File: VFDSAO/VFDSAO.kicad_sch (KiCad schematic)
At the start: 4 parts, among them U1 CH32V003FxPx, U2 HV5812, X1 Simple_Addon_v2

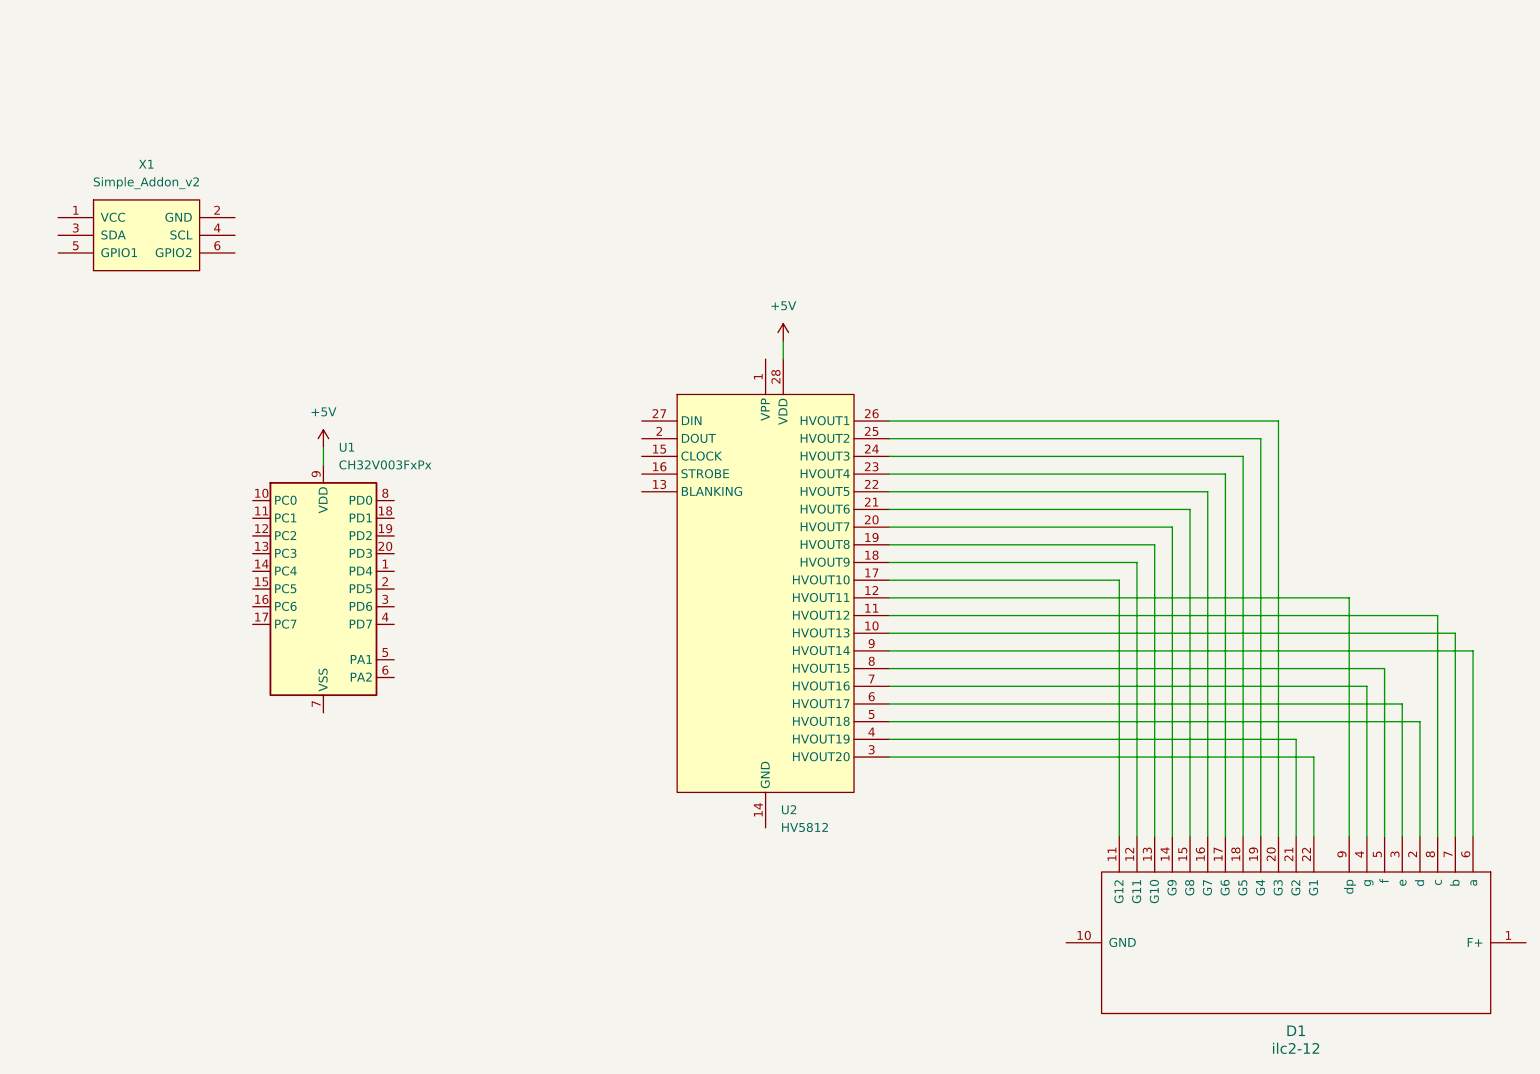
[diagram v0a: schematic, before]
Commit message: Adding I2C level shifters
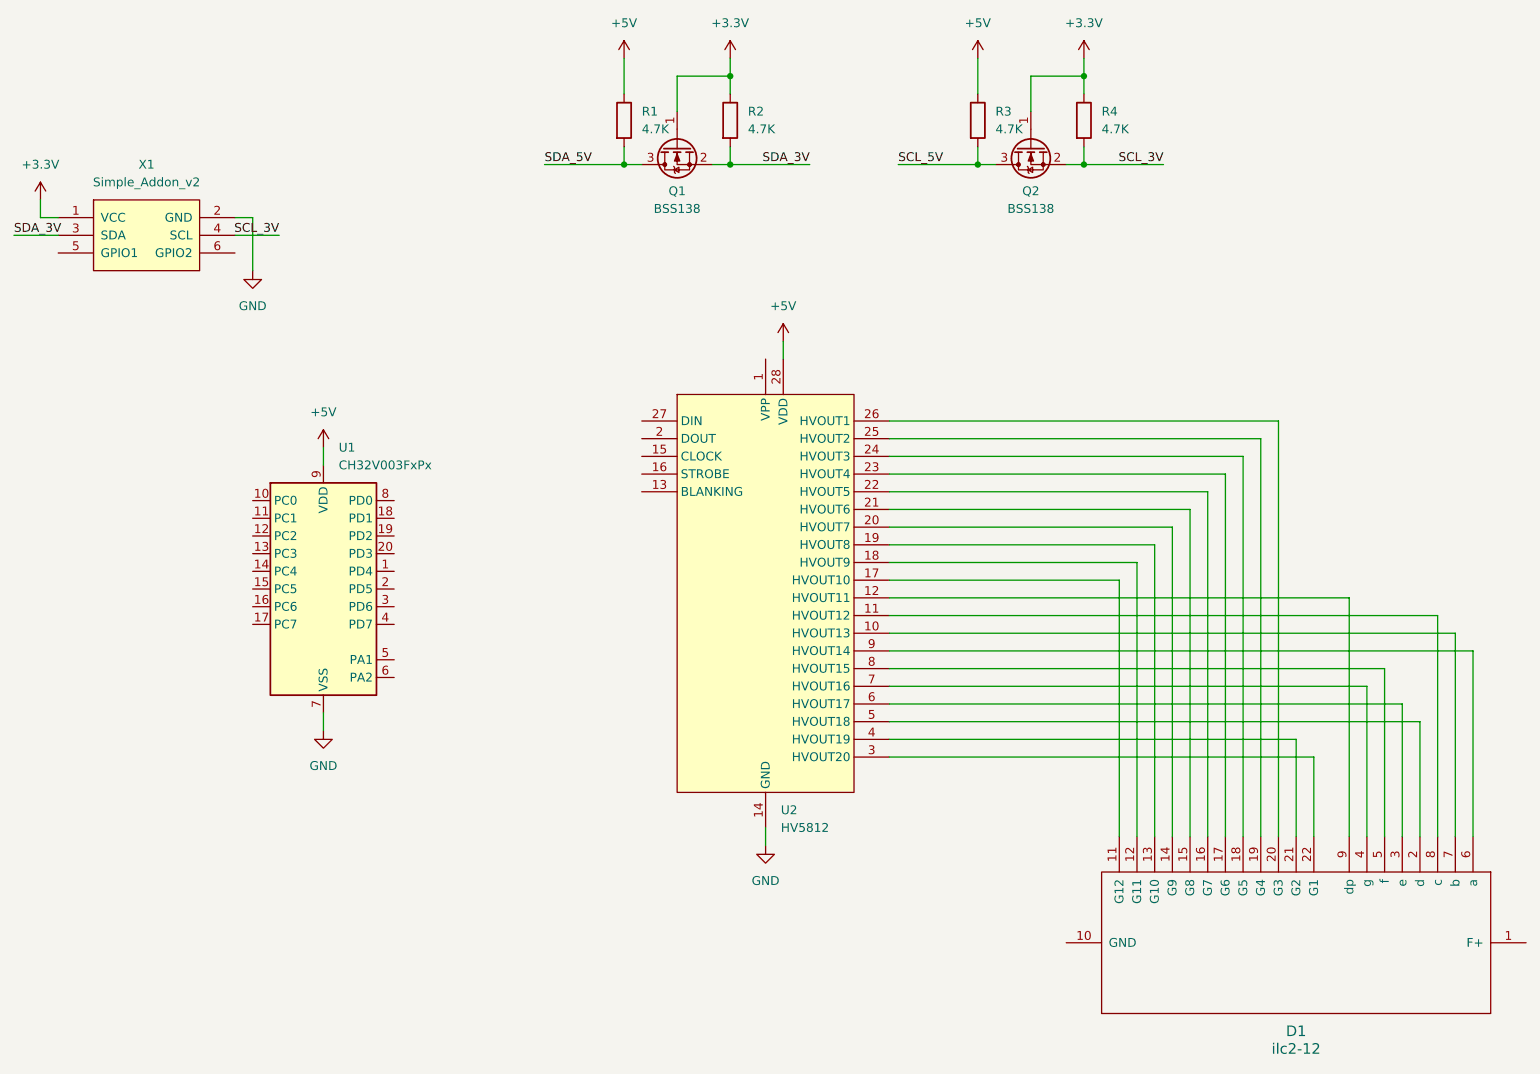
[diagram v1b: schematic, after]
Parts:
- added Q1, Q2: BSS138, Package_TO_SOT_SMD:SOT-23, symbol Transistor_FET:BSS138
- added R1, R2, R3, R4: 4.7K, symbol Device:R
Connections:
- net +5V: now also R1.1, R3.1
- net GND: now reaches U2.14 (GND)
- net GND: now also U1.7 (VSS), X1.2 (GND)
- net +3.3V: now reaches X1.1 (VCC)
- net +3.3V: now also Q1.1 (G), Q2.1 (G), R2.1, R4.1
- net SDA_3V: now reaches X1.3 (SDA)
- net SDA_3V: now also Q1.2 (S), R2.2
- net SCL_3V: now reaches X1.4 (SCL)
- net SCL_3V: now also Q2.2 (S), R4.2
- new net SCL_5V: Q2.3 (D), R3.2
- new net SDA_5V: Q1.3 (D), R1.2
